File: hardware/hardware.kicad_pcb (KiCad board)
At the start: 2 copper layers, 150 x 90 mm, 57 parts, among them U1 NE555P, U3 LM3914V

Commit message: more schematics
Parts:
- removed the R16 at (139.7, 61.0)
- removed the R17 at (147.3, 58.4)
- removed the R18 at (154.9, 61.0)
- removed RV10, RV11, RV12, RV13, RV14, RV15, RV16, RV17, RV18, RV19, RV20, RV21, RV6, RV7, RV8, RV9: 50, Potentiometer_THT:Potentiometer_ACP_CA9-V10_Vertical
- removed RV22, RV23, RV24, RV25: 10k, Potentiometer_THT:Potentiometer_Piher_T-16L_Single_Vertical_Hole
- removed RV26: 50k, Potentiometer_THT:Potentiometer_Piher_T-16L_Single_Vertical_Hole
- added KB1: keyboard, keyboard:keyboard, F.Cu at (92.5, 109.1)
- added R23: 220k, Resistor_THT:R_Axial_DIN0207_L6.3mm_D2.5mm_P10.16mm_Horizontal, F.Cu at (259.1, 71.1)
- added R25: 68, Resistor_THT:R_Axial_DIN0207_L6.3mm_D2.5mm_P10.16mm_Horizontal, F.Cu at (101.6, 81.3)
- added R26: 1.5k, Resistor_THT:R_Axial_DIN0207_L6.3mm_D2.5mm_P10.16mm_Horizontal, F.Cu at (104.1, 81.3)
- added R28: 1.6k, Resistor_THT:R_Axial_DIN0207_L6.3mm_D2.5mm_P10.16mm_Horizontal, F.Cu at (109.2, 81.3)
- added R29: 180, Resistor_THT:R_Axial_DIN0207_L6.3mm_D2.5mm_P10.16mm_Horizontal, F.Cu at (111.8, 81.3)
- added R30: 1.8k, Resistor_THT:R_Axial_DIN0207_L6.3mm_D2.5mm_P10.16mm_Horizontal, F.Cu at (114.3, 81.3)
- added R31: 0, Resistor_THT:R_Axial_DIN0207_L6.3mm_D2.5mm_P10.16mm_Horizontal, F.Cu at (116.8, 81.3)
- added R32: 1.8k, Resistor_THT:R_Axial_DIN0207_L6.3mm_D2.5mm_P10.16mm_Horizontal, F.Cu at (119.4, 81.3)
- added R33: 120, Resistor_THT:R_Axial_DIN0207_L6.3mm_D2.5mm_P10.16mm_Horizontal, F.Cu at (121.9, 81.3)
- added R34: 2.0k, Resistor_THT:R_Axial_DIN0207_L6.3mm_D2.5mm_P10.16mm_Horizontal, F.Cu at (202.5, 139.6)
- added R35: 160, Resistor_THT:R_Axial_DIN0207_L6.3mm_D2.5mm_P10.16mm_Horizontal, F.Cu at (202.5, 135.6)
- added R36: 2.2k, Resistor_THT:R_Axial_DIN0207_L6.3mm_D2.5mm_P10.16mm_Horizontal, F.Cu at (215.8, 139.6)
- added R37: 39, Resistor_THT:R_Axial_DIN0207_L6.3mm_D2.5mm_P10.16mm_Horizontal, F.Cu at (350.2, 100.4)
- added R38: 2.2k, Resistor_THT:R_Axial_DIN0207_L6.3mm_D2.5mm_P10.16mm_Horizontal, F.Cu at (229.1, 139.6)
- added R39: 30, Resistor_THT:R_Axial_DIN0207_L6.3mm_D2.5mm_P10.16mm_Horizontal, F.Cu at (350.2, 104.4)
- added R40: 2.7k, Resistor_THT:R_Axial_DIN0207_L6.3mm_D2.5mm_P10.16mm_Horizontal, F.Cu at (242.4, 131.5)
- added R41: 160, Resistor_THT:R_Axial_DIN0207_L6.3mm_D2.5mm_P10.16mm_Horizontal, F.Cu at (229.1, 135.6)
- added R42: 12k, Resistor_THT:R_Axial_DIN0207_L6.3mm_D2.5mm_P10.16mm_Horizontal, F.Cu at (363.5, 100.4)
- added R43: 240, Resistor_THT:R_Axial_DIN0207_L6.3mm_D2.5mm_P10.16mm_Horizontal, F.Cu at (202.5, 131.5)
- added R44: 10k, Resistor_THT:R_Axial_DIN0207_L6.3mm_D2.5mm_P10.16mm_Horizontal, F.Cu at (215.8, 135.6)
- added R45: 50k, Resistor_THT:R_Axial_DIN0207_L6.3mm_D2.5mm_P10.16mm_Horizontal, F.Cu at (215.8, 131.5)
- added R46: 10k, Resistor_THT:R_Axial_DIN0207_L6.3mm_D2.5mm_P10.16mm_Horizontal, F.Cu at (242.4, 135.6)
- added R47: 50k, Resistor_THT:R_Axial_DIN0207_L6.3mm_D2.5mm_P10.16mm_Horizontal, F.Cu at (350.2, 108.5)
- added R48: 100k, Resistor_THT:R_Axial_DIN0207_L6.3mm_D2.5mm_P10.16mm_Horizontal, F.Cu at (229.1, 131.5)
- added R62: 12k, Resistor_THT:R_Axial_DIN0207_L6.3mm_D2.5mm_P10.16mm_Horizontal, F.Cu at (147.3, 81.3)
- added R63: 240, Resistor_THT:R_Axial_DIN0207_L6.3mm_D2.5mm_P10.16mm_Horizontal, F.Cu at (149.9, 81.3)
- R10: value 1.3k -> 39
- R11: value 1.41k -> 1k
- R12: value 220k -> 0
- R13: value 1.37k -> 680
- R14: value 1.58k -> 47
- R15: value 1.79k -> 1k
- R16: renamed from R23; value 100k -> 30
- R17: renamed from R25; value 50k -> 1.1k
- R18: renamed from R26; value 10k -> 10
- R19: value 2.24k -> 1.3k
- R2: value 570 -> 0
- R20: value 2.23k -> 0
- R21: value 2.86k -> 1.3k
- R22: value 12.25k -> 110
- R24: value 10k -> 1.3k
- R27: value 50k -> 75
- R3: value 1.12k -> 560
- R4: value 600 -> 10
- R5: value 790 -> 1.1k
- R6: value 1k -> 20
- R7: value 730 -> 560
- R8: value 1.03k -> 39
- R9: value 1.11k -> 750
- RV1: value 200 -> 10k; footprint Potentiometer_THT:Potentiometer_ACP_CA9-V10_Vertical -> Potentiometer_THT:Potentiometer_Piher_T-16L_Single_Vertical_Hole
- RV2, RV3, RV5: value 50 -> 10k; footprint Potentiometer_THT:Potentiometer_ACP_CA9-V10_Vertical -> Potentiometer_THT:Potentiometer_Piher_T-16L_Single_Vertical_Hole
- RV4: value 50 -> 50k; footprint Potentiometer_THT:Potentiometer_ACP_CA9-V10_Vertical -> Potentiometer_THT:Potentiometer_Piher_T-16L_Single_Vertical_Hole
- moved R12 307.4 mm to (71.1, 81.3), turned to -90 degrees
- moved R16 295.7 mm to (81.3, 81.3), turned to -90 degrees
- moved R17 277.2 mm to (83.8, 81.3), turned to -90 degrees
- moved R24 246.8 mm to (99.1, 81.3), turned to -90 degrees
- moved R18 246.1 mm to (86.4, 81.3), turned to -90 degrees
- moved R27 236.6 mm to (106.7, 81.3), turned to -90 degrees
- moved RV3 198.0 mm to (164.3, -91.5), turned to 0 degrees
- moved RV1 197.3 mm to (169.4, -71.2), turned to 0 degrees
- moved A1 195.3 mm to (128.9, 24.1), turned to 0 degrees
- moved BAR1 175.4 mm to (218.4, 20.3)
- moved U3 175.4 mm to (222.2, 51.2)
- moved U1 175.4 mm to (229.7, 20.1)
- moved RV2 174.4 mm to (123.7, -99.1), turned to 0 degrees
- moved RV5 145.6 mm to (146.5, -50.9), turned to 0 degrees
- moved RV4 145.2 mm to (130.1, -70.0), turned to 0 degrees
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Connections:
- A1 pad 14: D_SYNTH -> unconnected-(A1-Pad14)
- A1 pad 26: unconnected-(A1-Pad26) -> D_SYNTH
- R1 pad 1: Net-(R1-Pad1) -> VCC
- R10 pad 2: Net-(R10-Pad2) -> PAD_A3
- R11 pad 1: Net-(R11-Pad1) -> PAD_A3
- R12 pad 1: A_SYNTH -> Net-(R11-Pad2)
- R12 pad 2: Net-(C3-Pad1) -> PAD_A#3
- R13 pad 1: Net-(R13-Pad1) -> PAD_A#3
- R14 pad 1: Net-(R14-Pad1) -> Net-(R13-Pad2)
- R14 pad 2: Net-(R14-Pad2) -> PAD_B3
- R15 pad 1: Net-(R15-Pad1) -> PAD_B3
- R16 pad 1: Net-(A1-Pad12) -> Net-(R15-Pad2)
- R16 pad 2: KB_IN -> PAD_C4
- R17 pad 1: Net-(R24-Pad2) -> PAD_C4
- R17 pad 2: AUDIO_OUT -> Net-(R17-Pad2)
- R18 pad 1: A_SYNTH_AMPF -> Net-(R17-Pad2)
- R18 pad 2: Net-(R26-Pad2) -> PAD_C#4
- R19 pad 1: Net-(R19-Pad1) -> PAD_C#4
- R2 pad 1: Net-(R2-Pad1) -> Net-(R1-Pad2)
- R2 pad 2: Net-(R2-Pad2) -> PAD_F3
- R20 pad 1: Net-(R20-Pad1) -> Net-(R19-Pad2)
- R20 pad 2: Net-(R20-Pad2) -> PAD_D4
- R21 pad 1: Net-(R21-Pad1) -> PAD_D4
- R22 pad 1: GND -> Net-(R21-Pad2)
- R22 pad 2: Net-(R22-Pad2) -> PAD_D#4
- R24 pad 1: D_SYNTH_AMPF -> PAD_D#4
- R27 pad 2: AUDIO_OUT -> PAD_F4
- R3 pad 1: Net-(R3-Pad1) -> PAD_F3
- R4 pad 1: Net-(R4-Pad1) -> Net-(R3-Pad2)
- R4 pad 2: Net-(R4-Pad2) -> PAD_F#3
- R5 pad 1: Net-(R5-Pad1) -> PAD_F#3
- R6 pad 1: Net-(R6-Pad1) -> Net-(R5-Pad2)
- R6 pad 2: Net-(R6-Pad2) -> PAD_G3
- R7 pad 1: Net-(R7-Pad1) -> PAD_G3
- R8 pad 1: Net-(R8-Pad1) -> Net-(R7-Pad2)
- R8 pad 2: Net-(R8-Pad2) -> PAD_G#3
- R9 pad 1: Net-(R9-Pad1) -> PAD_G#3
- R9 pad 2: Net-(R9-Pad2) -> Net-(R10-Pad1)
- RV1 pad 2: Net-(R1-Pad2) -> POT_ATK
- RV1 pad 3: unconnected-(RV1-Pad3) -> GND
- RV2 pad 1: Net-(R1-Pad1) -> VCC
- RV2 pad 2: Net-(R2-Pad2) -> POT_REL
- RV2 pad 3: unconnected-(RV2-Pad3) -> GND
- RV3 pad 1: Net-(R2-Pad1) -> VCC
- RV3 pad 2: Net-(R3-Pad2) -> POT_WAV
- RV3 pad 3: unconnected-(RV3-Pad3) -> GND
- RV4 pad 1: Net-(R3-Pad1) -> Net-(R44-Pad2)
- RV4 pad 2: Net-(R4-Pad2) -> GND
- RV4 pad 3: unconnected-(RV4-Pad3) -> Net-(R46-Pad2)
- RV5 pad 1: Net-(R4-Pad1) -> unconnected-(RV5-Pad1)
- RV5 pad 2: Net-(R5-Pad2) -> unconnected-(RV5-Pad2)
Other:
- board size 150 x 90 mm -> 150 x 107.8 mm

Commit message: more schematics
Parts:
- added J1: USB_B, Connector_USB:USB_B_Lumberg_2411_02_Horizontal, F.Cu at (36.9, 32.2)
- added J2: AUDIO, Connector_Audio:Jack_3.5mm_Ledino_KB3SPRS_Horizontal, F.Cu at (152.8, 25.8)
- added J3: STYLUS, Connector_Audio:Jack_3.5mm_Ledino_KB3SPRS_Horizontal, F.Cu at (164.8, 63.9)
- A1: moved to B.Cu
- RV1, RV2, RV3, RV4, RV5: footprint Potentiometer_THT:Potentiometer_Piher_T-16L_Single_Vertical_Hole -> keyboard:potm
- moved R37 218.9 mm to (132.1, 81.3), turned to -90 degrees
- moved R39 214.3 mm to (137.2, 81.3), turned to -90 degrees
- moved R42 204.3 mm to (160.0, 81.3), turned to -90 degrees
- moved RV1 184.6 mm to (35.6, 55.9), turned to 90 degrees
- moved RV3 171.7 mm to (76.2, 55.9), turned to 90 degrees
- moved RV2 169.2 mm to (55.8, 55.9), turned to 90 degrees
- moved BAR1 136.4 mm to (85.2, 49.4), turned to 90 degrees
- moved RV4 126.7 mm to (144.7, 55.9), turned to 90 degrees
- moved R47 119.6 mm to (231.1, 96.5)
- moved U1 118.8 mm to (120.7, 67.3)
- moved U3 118.3 mm to (104.1, 58.4), turned to 90 degrees
- moved R40 114.4 mm to (139.7, 81.3), turned to -90 degrees
- moved R38 111.1 mm to (134.6, 81.3), turned to -90 degrees
- moved RV5 108.3 mm to (165.0, 55.9), turned to 90 degrees
- moved R36 104.1 mm to (129.5, 81.3), turned to -90 degrees
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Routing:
- net GND: track 0.00 -> 185.9 mm
- net VCC: track 0.00 -> 104.2 mm
- net PAD_F3: track 0.00 -> 62.2 mm
- net PAD_B4: track 0.00 -> 59.4 mm
- net PAD_G3: track 0.00 -> 59.3 mm
- net POT_ATK: track 0.00 -> 58.1 mm
- net PAD_A4: track 0.00 -> 55.7 mm
- net PAD_G4: track 0.00 -> 52.9 mm
- net PAD_C4: track 0.00 -> 48.8 mm
- net PAD_D4: track 0.00 -> 45.8 mm
- net PAD_F4: track 0.00 -> 45.6 mm
- net PAD_E4: track 0.00 -> 44.8 mm
- net PAD_F#3: track 0.00 -> 43.9 mm
- net POT_REL: track 0.00 -> 40.4 mm
- net PAD_G#3: track 0.00 -> 40.4 mm
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
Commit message: more hardware
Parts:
- removed R62: 12k, Resistor_THT:R_Axial_DIN0207_L6.3mm_D2.5mm_P10.16mm_Horizontal
- removed R63: 240, Resistor_THT:R_Axial_DIN0207_L6.3mm_D2.5mm_P10.16mm_Horizontal
- U3: footprint Package_LCC:PLCC-20 -> keyboard:avans-lm3914v
- moved R23 127.1 mm to (132.1, 66.0), turned to -90 degrees
- moved R44 118.9 mm to (119.4, 61.0)
- moved R45 118.9 mm to (119.4, 58.4)
- moved R46 118.9 mm to (119.4, 53.3)
- moved R47 118.9 mm to (119.4, 55.9)
- moved R48 86.7 mm to (142.2, 73.7)
- moved U3 8.03 mm to (96.5, 61.0)
- moved BAR1 1.38 mm to (83.8, 49.4)

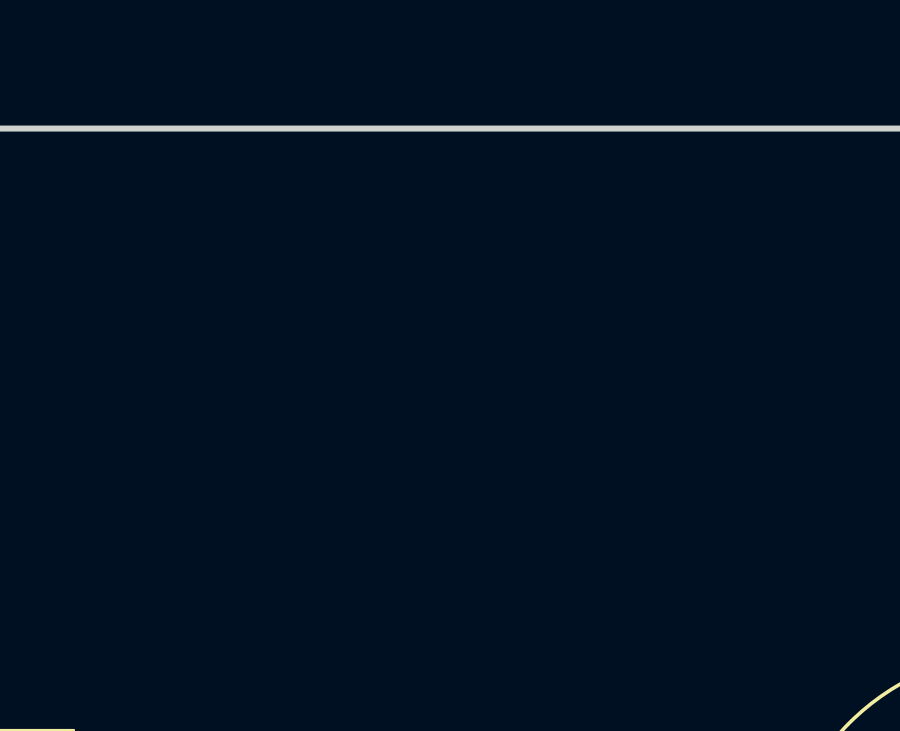
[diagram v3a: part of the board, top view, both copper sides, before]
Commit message: more hardware
amplifier circuit done
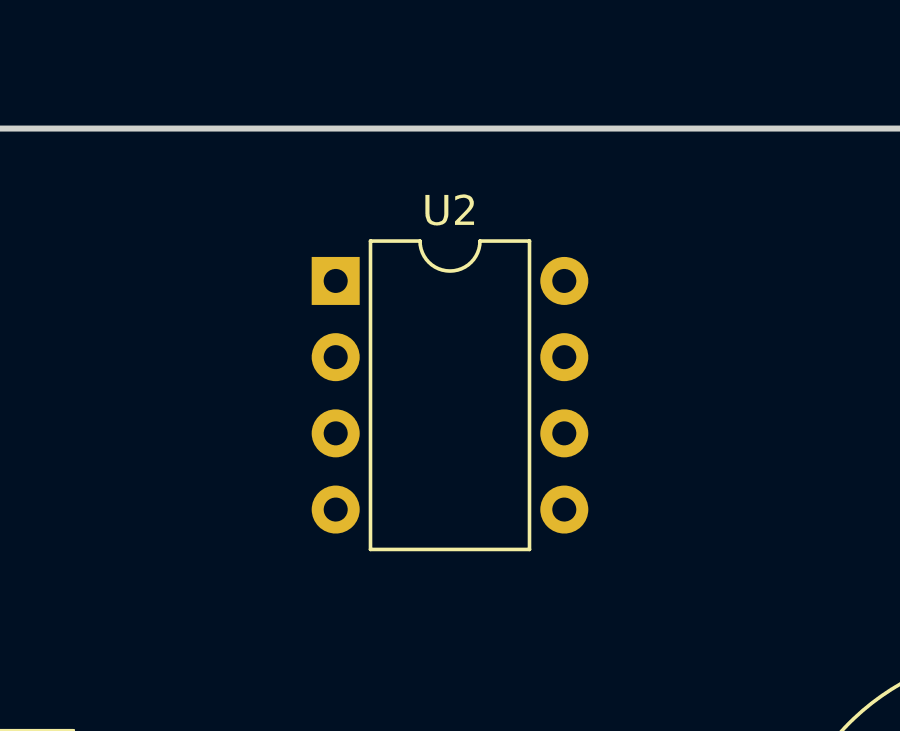
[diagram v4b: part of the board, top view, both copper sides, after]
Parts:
- added U2: LM386, Package_DIP:DIP-8_W7.62mm, F.Cu at (116.8, 25.4)
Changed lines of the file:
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@@
   (net 98 "unconnected-(J1-Pad2)")
   (net 99 "unconnected-(J1-Pad3)")
+  (net 100 "unconnected-(U2-Pad1)")
+  (net 101 "unconnected-(U2-Pad2)")
+  (net 102 "unconnected-(U2-Pad3)")
+  (net 103 "Net-(C5-Pad1)")
+  (net 104 "unconnected-(U2-Pad7)")
+  (net 105 "unconnected-(U2-Pad8)")
   (footprint "Resistor_THT:R_Axial_DIN0207_L6.3mm_D2.5mm_P10.16mm_Horizontal" (layer "F.Cu")
     (at 119.38 58.42)
@@
       (net 63 "unconnected-(RV5-Pad3)") (pinfunction "3") (pintype "passive"))
   )
+  (footprint "Package_DIP:DIP-8_W7.62mm" (layer "F.Cu")
+    (at 116.84 25.4)
+    (descr "8-lead though-hole mounted DIP package, row spacing 7.62 mm (300 mils)")
+    (tags "THT DIP DIL PDIP 2.54mm 7.62mm 300mil")
+    (property "Sheetfile" "hardware.kicad_sch")
+    (property "Sheetname" "")
+    (attr through_hole)
+    (fp_text reference "U2" (at 3.81 -2.33) (layer "F.SilkS")
+      (effects (font (size 1 1) (thickness 0.15)))
+    )
+    (fp_text value "LM386" (at 3.81 9.95) (layer "F.Fab")
+      (effects (font (size 1 1) (thickness 0.15)))
+    )
+    (fp_text user "${REFERENCE}" (at 3.81 3.81) (layer "F.Fab")
+      (effects (font (size 1 1) (thickness 0.15)))
+    )
+    (fp_line (start 6.46 -1.33) (end 4.81 -1.33) (layer "F.SilkS") (width 0.12))
+    (fp_line (start 6.46 8.95) (end 6.46 -1.33) (layer "F.SilkS") (width 0.12))
+    (fp_line (start 1.16 -1.33) (end 1.16 8.95) (layer "F.SilkS") (width 0.12))
+    (fp_line (start 2.81 -1.33) (end 1.16 -1.33) (layer "F.SilkS") (width 0.12))
+    (fp_line (start 1.16 8.95) (end 6.46 8.95) (layer "F.SilkS") (width 0.12))
+    (fp_arc (start 4.81 -1.33) (mid 3.81 -0.33) (end 2.81 -1.33) (layer "F.SilkS") (width 0.12))
+    (fp_line (start 8.7 9.15) (end 8.7 -1.55) (layer "F.CrtYd") (width 0.05))
+    (fp_line (start -1.1 -1.55) (end -1.1 9.15) (layer "F.CrtYd") (width 0.05))
+    (fp_line (start -1.1 9.15) (end 8.7 9.15) (layer "F.CrtYd") (width 0.05))
+    (fp_line (start 8.7 -1.55) (end -1.1 -1.55) (layer "F.CrtYd") (width 0.05))
+    (fp_line (start 1.635 -1.27) (end 6.985 -1.27) (layer "F.Fab") (width 0.1))
+    (fp_line (start 6.985 -1.27) (end 6.985 8.89) (layer "F.Fab") (width 0.1))
+    (fp_line (start 0.635 8.89) (end 0.635 -0.27) (layer "F.Fab") (width 0.1))
+    (fp_line (start 0.635 -0.27) (end 1.635 -1.27) (layer "F.Fab") (width 0.1))
+    (fp_line (start 6.985 8.89) (end 0.635 8.89) (layer "F.Fab") (width 0.1))
+    (pad "1" thru_hole rect (at 0 0) (size 1.6 1.6) (drill 0.8) (layers *.Cu *.Mask)
+      (net 100 "unconnected-(U2-Pad1)") (pinfunction "GAIN") (pintype "input"))
+    (pad "2" thru_hole oval (at 0 2.54) (size 1.6 1.6) (drill 0.8) (layers *.Cu *.Mask)
+      (net 101 "unconnected-(U2-Pad2)") (pinfunction "-") (pintype "input"))
+    (pad "3" thru_hole oval (at 0 5.08) (size 1.6 1.6) (drill 0.8) (layers *.Cu *.Mask)
+      (net 102 "unconnected-(U2-Pad3)") (pinfunction "+") (pintype "input"))
+    (pad "4" thru_hole oval (at 0 7.62) (size 1.6 1.6) (drill 0.8) (layers *.Cu *.Mask)
+      (net 6 "GND") (pinfunction "GND") (pintype "power_in"))
+    (pad "5" thru_hole oval (at 7.62 7.62) (size 1.6 1.6) (drill 0.8) (layers *.Cu *.Mask)
+      (net 103 "Net-(C5-Pad1)") (pintype "output"))
+    (pad "6" thru_hole oval (at 7.62 5.08) (size 1.6 1.6) (drill 0.8) (layers *.Cu *.Mask)
+      (net 5 "VCC") (pinfunction "V+") (pintype "power_in"))
+    (pad "7" thru_hole oval (at 7.62 2.54) (size 1.6 1.6) (drill 0.8) (layers *.Cu *.Mask)
+      (net 104 "unconnected-(U2-Pad7)") (pinfunction "BYPASS") (pintype "input"))
+    (pad "8" thru_hole oval (at 7.62 0) (size 1.6 1.6) (drill 0.8) (layers *.Cu *.Mask)
+      (net 105 "unconnected-(U2-Pad8)") (pinfunction "GAIN") (pintype "input"))
+    (model "${KICAD6_3DMODEL_DIR}/Package_DIP.3dshapes/DIP-8_W7.62mm.wrl"
+      (offset (xyz 0 0 0))
+      (scale (xyz 1 1 1))
+      (rotate (xyz 0 0 0))
+    )
+  )
   (footprint "Connector_Audio:Jack_3.5mm_Ledino_KB3SPRS_Horizontal" (layer "F.Cu")

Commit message: more hardware (almost done!)
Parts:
- moved U3 46.0 mm to (135.9, 67.3)
- moved R50 8.03 mm to (149.9, 76.2), turned to 90 degrees
- moved U1 5.08 mm to (115.6, 67.3)
- moved R23 2.54 mm to (129.5, 66.0)
- renumbered R48 to R50, U3 to U2, U2 to U3
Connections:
- A1 pad 26: D_SYNTH -> Net-(A1-Pad26)
- RV5 pad 2: unconnected-(RV5-Pad2) -> Net-(RV5-Pad2)
- RV5 pad 3: unconnected-(RV5-Pad3) -> Net-(RV5-Pad3)
- U2 pad 5: AUDIO_OUT -> Net-(C6-Pad1)
- U3 pad 1: unconnected-(U2-Pad1) -> Net-(RV5-Pad2)
- U3 pad 2: unconnected-(U2-Pad2) -> GND
- U3 pad 3: unconnected-(U2-Pad3) -> PRE_AMP
- U3 pad 8: unconnected-(U2-Pad8) (its old number) -> Net-(RV5-Pad3)
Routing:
- net Net-(BAR1-Pad19): track 0.00 -> 72.1 mm
- net Net-(BAR1-Pad18): track 0.00 -> 65.1 mm
- net Net-(BAR1-Pad17): track 0.00 -> 57.9 mm
- net Net-(BAR1-Pad16): track 0.00 -> 50.9 mm
- net Net-(BAR1-Pad15): track 0.00 -> 44.0 mm
- net Net-(BAR1-Pad14): track 0.00 -> 37.0 mm
- net Net-(BAR1-Pad13): track 0.00 -> 29.8 mm
- net Net-(BAR1-Pad20): track 0.00 -> 29.0 mm
- net VCC: track 104.2 -> 131.2 mm
- net Net-(BAR1-Pad1): track 0.00 -> 22.9 mm
- net Net-(BAR1-Pad12): track 0.00 -> 22.2 mm
- net GND: track 185.9 -> 167.9 mm
- net Net-(BAR1-Pad11): track 0.00 -> 12.6 mm

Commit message: more hardware
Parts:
- BAR1: value HDSP-4832_2 -> HDSP-4832
- moved BAR1 24.0 mm to (106.7, 42.0), turned to -90 degrees
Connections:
- BAR1 pad 1: Net-(BAR1-Pad1) -> VCC
- BAR1 pad 10: Net-(BAR1-Pad1) -> VCC
- BAR1 pad 2: Net-(BAR1-Pad1) -> VCC
- BAR1 pad 3: Net-(BAR1-Pad1) -> VCC
- BAR1 pad 4: Net-(BAR1-Pad1) -> VCC
- BAR1 pad 5: Net-(BAR1-Pad1) -> VCC
- BAR1 pad 6: Net-(BAR1-Pad1) -> VCC
- BAR1 pad 7: Net-(BAR1-Pad1) -> VCC
- BAR1 pad 8: Net-(BAR1-Pad1) -> VCC
- BAR1 pad 9: Net-(BAR1-Pad1) -> VCC
- U2 pad 1: Net-(BAR1-Pad20) -> Net-(BAR1-Pad11)
- U2 pad 10: unconnected-(U2-Pad10) -> Net-(U2-Pad10)
- U2 pad 12: Net-(BAR1-Pad11) -> Net-(BAR1-Pad20)
- U2 pad 13: Net-(BAR1-Pad12) -> Net-(BAR1-Pad19)
- U2 pad 14: Net-(BAR1-Pad13) -> Net-(BAR1-Pad18)
- U2 pad 15: Net-(BAR1-Pad14) -> Net-(BAR1-Pad17)
- U2 pad 16: Net-(BAR1-Pad15) -> Net-(BAR1-Pad16)
- U2 pad 17: Net-(BAR1-Pad16) -> Net-(BAR1-Pad15)
- U2 pad 18: Net-(BAR1-Pad17) -> Net-(BAR1-Pad14)
- U2 pad 19: Net-(BAR1-Pad18) -> Net-(BAR1-Pad13)
- U2 pad 20: Net-(BAR1-Pad19) -> Net-(BAR1-Pad12)
- U2 pad 6: unconnected-(U2-Pad6) -> Net-(U2-Pad6)
- U2 pad 8: unconnected-(U2-Pad8) -> Net-(U2-Pad6)
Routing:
- net Net-(BAR1-Pad19): track 72.1 -> 3.70 mm
- net Net-(BAR1-Pad18): track 65.1 -> 3.70 mm
- net Net-(BAR1-Pad17): track 57.9 -> 3.70 mm
- net Net-(BAR1-Pad16): track 50.9 -> 3.70 mm
- net Net-(BAR1-Pad15): track 44.0 -> 3.70 mm
- net VCC: track 131.2 -> 170.1 mm
- net Net-(BAR1-Pad14): track 37.0 -> 3.70 mm
- net Net-(BAR1-Pad13): track 29.8 -> 3.70 mm
- net Net-(BAR1-Pad20): track 29.0 -> 3.70 mm
- net Net-(BAR1-Pad1): track 22.9 -> 0.00 mm
- net Net-(BAR1-Pad12): track 22.2 -> 3.70 mm
- net Net-(BAR1-Pad11): track 12.6 -> 20.0 mm

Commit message: more hardware
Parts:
- added C1: 100n, Capacitor_THT:C_Disc_D3.0mm_W1.6mm_P2.50mm, F.Cu at (119.4, 71.1)
- added C10: 2.2u, Capacitor_THT:CP_Radial_D5.0mm_P2.00mm, F.Cu at (81.3, 59.7)
- added C11: 10n, Capacitor_THT:C_Disc_D3.0mm_W1.6mm_P2.50mm, F.Cu at (76.2, 30.5)
- added C12: 100n, Capacitor_THT:C_Disc_D3.0mm_W1.6mm_P2.50mm, F.Cu at (25.4, 25.4)
- added C2: 100n, Capacitor_THT:C_Disc_D3.0mm_W1.6mm_P2.50mm, F.Cu at (134.6, 71.1)
- added C3: 10n, Capacitor_THT:C_Disc_D3.0mm_W1.6mm_P2.50mm, F.Cu at (134.6, 68.6)
- added C4: 100n, Capacitor_THT:C_Disc_D3.0mm_W1.6mm_P2.50mm, F.Cu at (88.9, 66.0)
- added C5: 100n, Capacitor_THT:C_Disc_D3.0mm_W1.6mm_P2.50mm, F.Cu at (130.8, 29.2)
- added C6: 1u, Capacitor_THT:CP_Radial_D5.0mm_P2.00mm, F.Cu at (111.8, 73.7)
- added C7: 1u, Capacitor_THT:CP_Radial_D5.0mm_P2.00mm, F.Cu at (139.7, 76.2)
- added C8: 100u, Capacitor_THT:CP_Radial_D10.0mm_P2.50mm, F.Cu at (144.8, 66.0)
- added C9: 10u, Capacitor_THT:CP_Radial_D10.0mm_P2.50mm, F.Cu at (83.8, 33.0)
- added D1: D, Diode_THT:D_A-405_P7.62mm_Horizontal, F.Cu at (96.5, 71.1)
- added R48: 100k, Resistor_THT:R_Axial_DIN0207_L6.3mm_D2.5mm_P10.16mm_Horizontal, F.Cu at (96.5, 73.7)
- added R49: 1k, Resistor_THT:R_Axial_DIN0207_L6.3mm_D2.5mm_P10.16mm_Horizontal, F.Cu at (76.2, 33.0)
- added RV6: 4k7, Potentiometer_THT:Potentiometer_Piher_PT-10-V10_Vertical, F.Cu at (43.3, 73.8)
- moved U3 45.8 mm to (120.7, 24.1)
- moved R46 33.0 mm to (106.7, 22.9)
- moved R47 33.0 mm to (106.7, 25.4)
- moved R44 33.0 mm to (106.7, 30.5)
- moved R45 33.0 mm to (106.7, 27.9)
- moved R50 31.4 mm to (123.2, 59.7), turned to 0 degrees
- moved R23 10.9 mm to (123.2, 74.9), turned to 0 degrees
- moved U1 9.67 mm to (124.5, 63.5)

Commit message: hardware done
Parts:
- added J1: PJ_AKI, Connector_PinHeader_2.54mm:PinHeader_1x02_P2.54mm_Vertical, F.Cu at (152.4, 76.2)
- added J2: PJ_AAO, Connector_PinHeader_2.54mm:PinHeader_1x02_P2.54mm_Vertical, F.Cu at (118.1, 68.6)
- added J5: PJ_PAO, Connector_PinHeader_2.54mm:PinHeader_1x02_P2.54mm_Vertical, F.Cu at (147.3, 25.4)
- added J7: PJ_DAI, Connector_PinHeader_2.54mm:PinHeader_1x02_P2.54mm_Vertical, F.Cu at (142.2, 73.7)
- added J8: PJ_MAO, Connector_PinHeader_2.54mm:PinHeader_1x02_P2.54mm_Vertical, F.Cu at (109.2, 30.5)
- added J9: PJ_AAI, Connector_PinHeader_2.54mm:PinHeader_1x02_P2.54mm_Vertical, F.Cu at (139.7, 73.7)
- added SW1: SW_POWER, Button_Switch_THT:SW_Slide_1P2T_CK_OS102011MS2Q, F.Cu at (119.4, 43.7)
- moved C5 86.4 mm to (110.5, 40.6), turned to -90 degrees
- moved R49 56.4 mm to (139.7, 68.6), turned to 90 degrees
- moved R47 52.1 mm to (142.2, 68.6), turned to 90 degrees
- moved R48 48.8 mm to (144.8, 58.4), turned to -90 degrees
- moved R50 44.9 mm to (137.2, 58.4), turned to -90 degrees
- moved C8 43.5 mm to (144.8, 33.0)
- moved C9 38.8 mm to (137.2, 28.0), turned to -90 degrees
- moved U3 6.48 mm to (114.3, 25.4)
- moved C6 4.02 mm to (127.0, 30.5), turned to 180 degrees
- moved C2 3.80 mm to (130.8, 71.1)
- moved C3 3.80 mm to (130.8, 68.6)
- moved C1 3.80 mm to (115.6, 71.1)
- moved R23 3.80 mm to (119.4, 74.9)
- moved R46 3.80 mm to (119.4, 59.7)
- moved U1 3.80 mm to (120.7, 63.5)
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- renumbered C9 to C10, C10 to C11, C11 to C12, C12 to C5, C5 to C6, C6 to C7, C7 to C8, C8 to C9, J1 to J3, J3 to J4, J2 to J6, R48 to R44, R49 to R45, R50 to R46, R44 to R47, R45 to R48, R46 to R49, R47 to R50, RV6 to RV4, RV4 to RV6
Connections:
- C2 pad 1: KB_IN -> Net-(C2-Pad1)
- C8 pad 2: AUDIO_OUT -> Net-(C8-Pad2)
- J6 pad T: AUDIO_OUT -> Net-(C8-Pad2)
- R23 pad 1: A_SYNTH -> Net-(J2-Pad1)
- R47 pad 1: D_SYNTH -> Net-(J7-Pad2)
- R48 pad 2: PRE_AMP -> Net-(J8-Pad1)
- R49 pad 1: A_SYNTH -> Net-(J9-Pad2)
- R50 pad 2: PRE_AMP -> Net-(J8-Pad1)
- U1 pad 3: A_SYNTH -> Net-(J2-Pad1)
- U1 pad 5: KB_IN -> Net-(C2-Pad1)
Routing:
- net GND: track 167.9 -> 458.4 mm, vias 0 -> 2
- net VCC: track 170.1 -> 298.8 mm, vias 0 -> 1
- net Net-(J3-Pad1): track 0.00 -> 87.3 mm
- net D_SYNTH: track 0.00 -> 84.1 mm
- net AUDIO_OUT: track 0.00 -> 68.6 mm, vias 0 -> 2
- net Net-(RV4-Pad1): track 0.00 -> 65.7 mm
- net Net-(J8-Pad1): track 0.00 -> 65.3 mm
- net Net-(RV5-Pad2): track 0.00 -> 63.1 mm
- net KB_IN: track 0.00 -> 59.1 mm
- net Net-(RV4-Pad2): track 0.00 -> 57.8 mm, vias 0 -> 6
- net Net-(RV5-Pad3): track 0.00 -> 49.5 mm
- net Net-(A1-Pad12): track 0.00 -> 36.6 mm
- net A_SYNTH: track 0.00 -> 29.6 mm
- net Net-(C8-Pad1): track 0.00 -> 29.0 mm, vias 0 -> 2
- net Net-(C2-Pad1): track 0.00 -> 23.7 mm
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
